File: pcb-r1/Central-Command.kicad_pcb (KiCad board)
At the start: 4 copper layers, 38.1 x 63.5 mm, 58 parts, among them P101 CONN_01X10, P102 CONN_01X10, P103 CONN_01X04, P104 CONN_01X02, P105 CONN_01X04, P106 CONN_01X02, P201 CONN_01X06, P202 CONN_01X04, P203 CONN_01X04, P204 CONN_01X03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

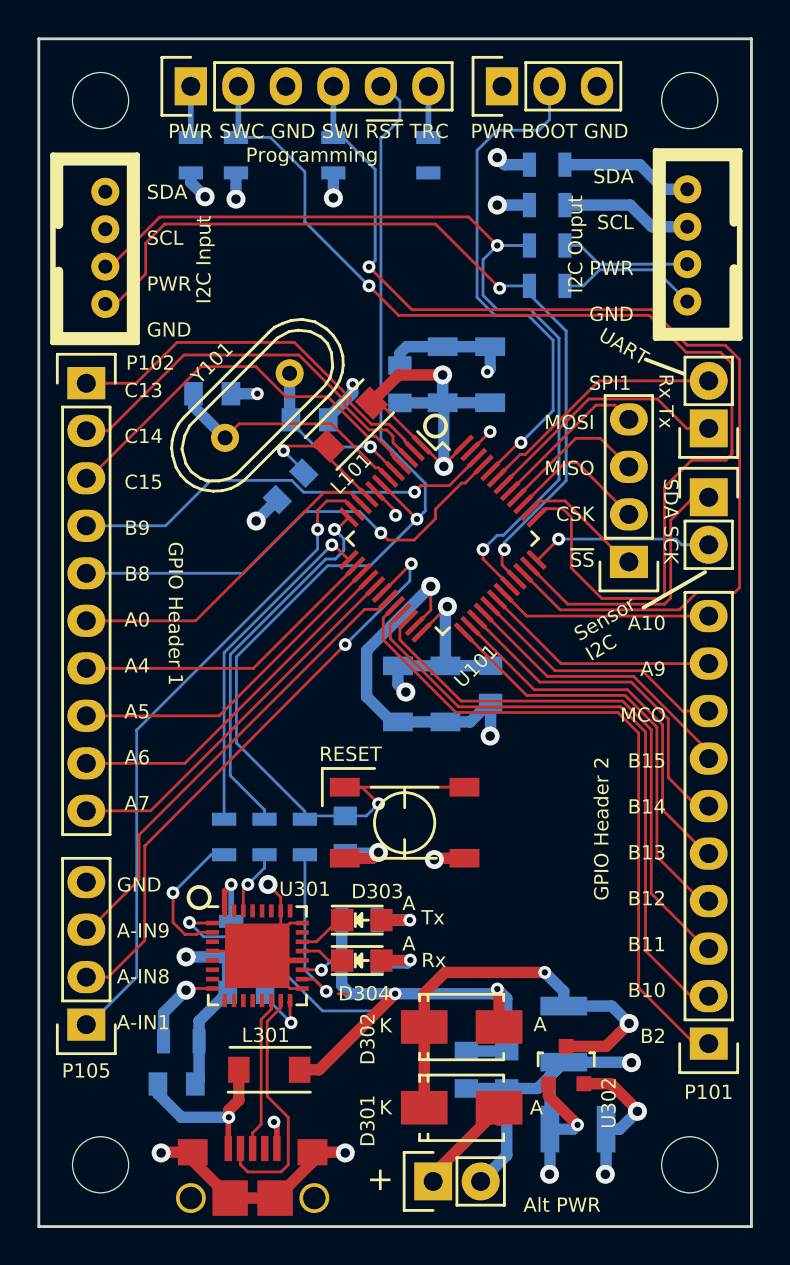
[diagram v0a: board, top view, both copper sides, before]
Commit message: Generated the final Gerbers for fabrication
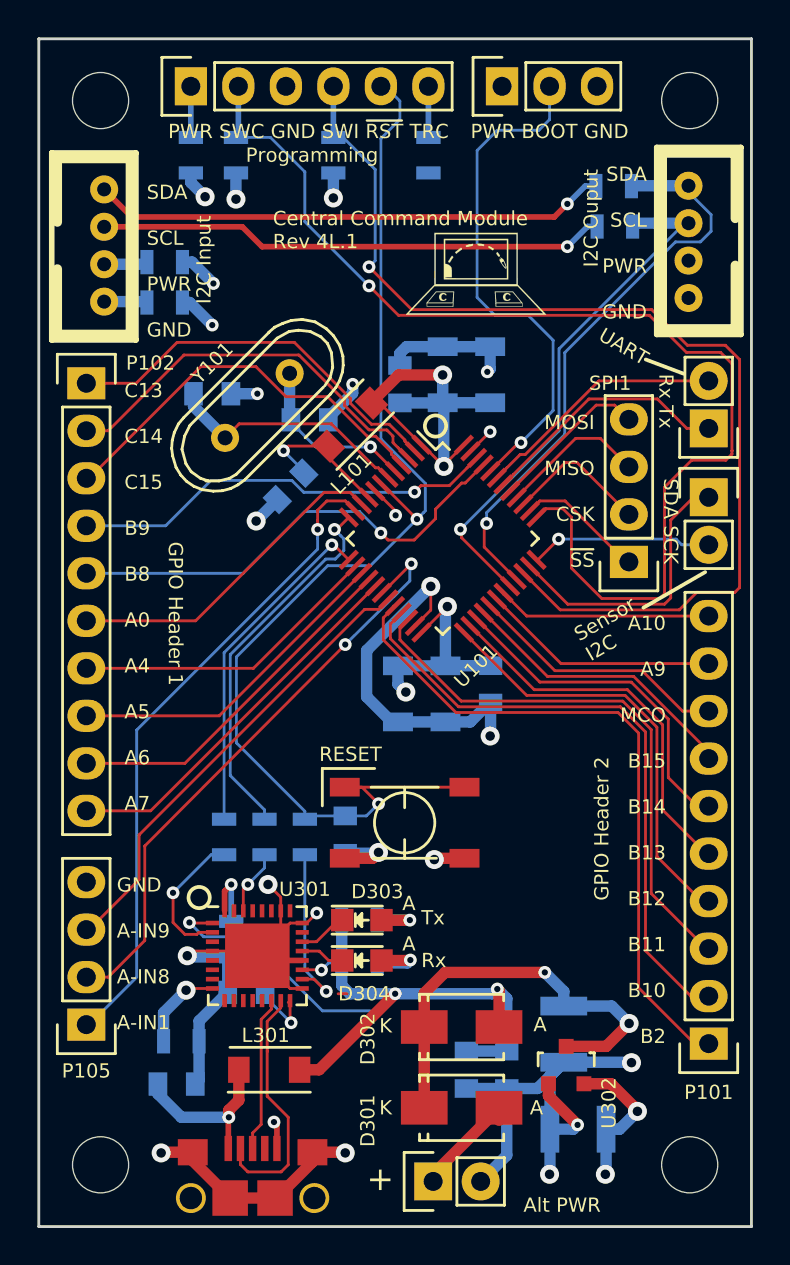
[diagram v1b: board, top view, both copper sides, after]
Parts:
- added G***: LOGO, CentralCommand:logo2, B.Cu at (102.5, 121.0)
- added G***: LOGO, CentralCommand:logo3, F.Cu at (99.6, 88.7)
- moved P203 31.8 mm to (79.7, 84.2), turned to 270 degrees
- moved P202 31.7 mm to (110.9, 90.1), turned to 90 degrees
- moved R206 21.7 mm to (82.9, 90.3), turned to 0 degrees
- moved R207 20.7 mm to (82.9, 88.1), turned to 0 degrees
- moved R209 6.41 mm to (106.9, 84.1), turned to 0 degrees
- moved R208 3.76 mm to (107.0, 86.2), turned to 0 degrees
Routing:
- net Net-(P203-Pad2): track 6.96 -> 27.5 mm, vias 0 -> 1
- net Net-(P203-Pad1): track 7.60 -> 27.6 mm, vias 0 -> 1
- net /Comm/SCL: track 48.2 -> 29.7 mm, vias 2 -> 1
- net /Comm/SDA: track 45.8 -> 31.1 mm, vias 2 -> 1
- net Net-(P203-Pad3): track 7.76 -> 2.62 mm
- net Net-(P203-Pad4): track 7.09 -> 3.50 mm
- net GND: track 109.4 -> 112.9 mm, vias 20 -> 21

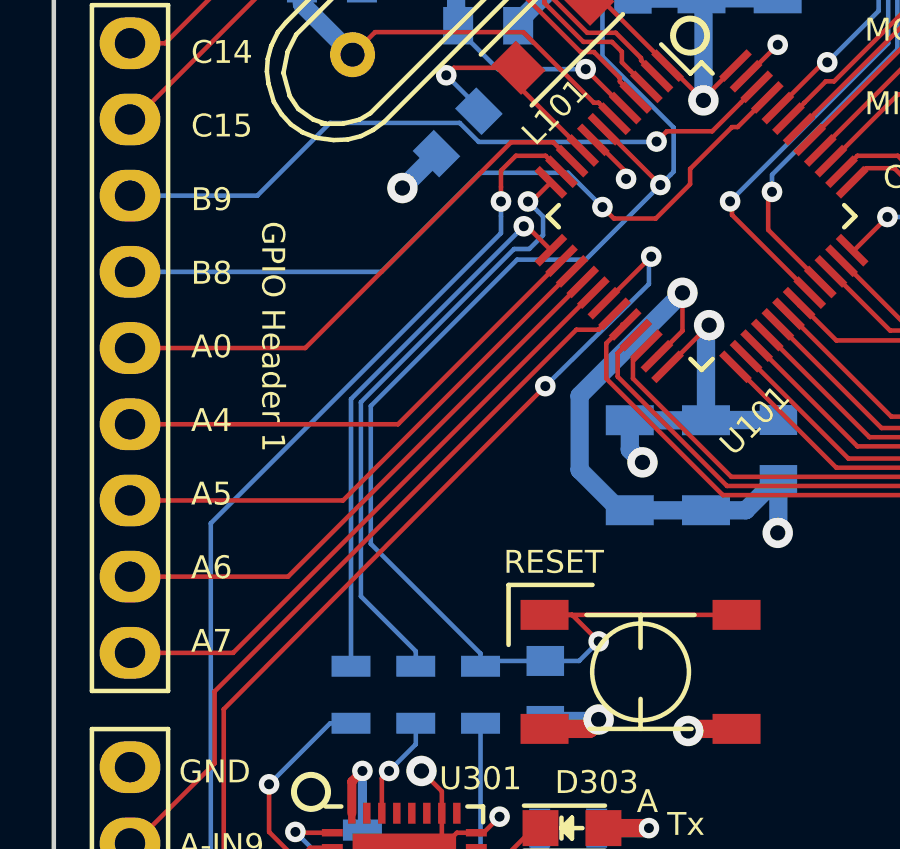
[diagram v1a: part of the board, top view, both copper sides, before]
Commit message: Corrected the routing of the Tx and Rx
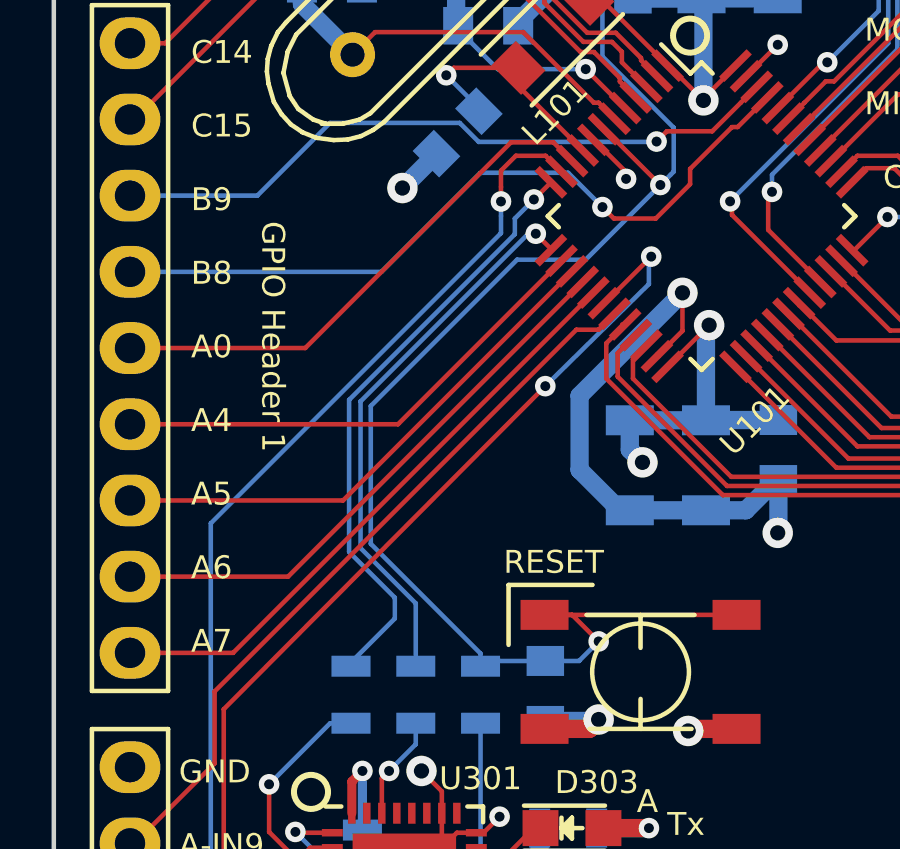
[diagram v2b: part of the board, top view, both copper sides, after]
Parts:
- C101, C201: value C -> 0.1μF
- C301: value 0.01μF -> 0.1μF
- R201, R202: value R -> 10kΩ
- R204: value 0Ω -> 10kΩ
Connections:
- U101 pad 12: /Power/TXD -> /Power/RXD
- U101 pad 13: /Power/RXD -> /Power/TXD
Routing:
- net /Power/RXD: track 18.3 -> 20.2 mm
- net /Power/TXD: track 20.6 -> 18.9 mm
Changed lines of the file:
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@@
     (thickness 1.6)
     (drawings 37)
-    (tracks 685)
+    (tracks 687)
     (zones 0)
     (modules 60)
@@
       (net 34 /ADC_IN1))
     (pad 12 smd rect (at -4.35 2.75 315) (size 1.3 0.25) (layers F.Cu F.Paste F.Mask)
-      (net 49 /Power/TXD))
-    (pad 13 smd rect (at -2.75 4.35 45) (size 1.3 0.25) (layers F.Cu F.Paste F.Mask)
       (net 51 /Power/RXD))
+    (pad 13 smd rect (at -2.75 4.35 45) (size 1.3 0.25) (layers F.Cu F.Paste F.Mask)
+      (net 49 /Power/TXD))
     (pad 14 smd rect (at -2.25 4.35 45) (size 1.3 0.25) (layers F.Cu F.Paste F.Mask)
       (net 27 "Net-(P102-Pad7)"))
@@
       (effects (font (size 0.762 0.762) (thickness 0.127)) (justify mirror))
     )
-    (fp_text value C (at 0 -2.1 225) (layer B.Fab)
+    (fp_text value 0.1μF (at 0 -2.1 225) (layer B.Fab)
       (effects (font (size 0.762 0.762) (thickness 0.127)) (justify mirror))
     )
@@
       (effects (font (size 0.762 0.762) (thickness 0.127)) (justify mirror))
     )
-    (fp_text value C (at 0 -2.1 270) (layer B.Fab)
+    (fp_text value 0.1μF (at 0 -2.1 270) (layer B.Fab)
       (effects (font (size 0.762 0.762) (thickness 0.127)) (justify mirror))
     )
@@
       (effects (font (size 0.762 0.762) (thickness 0.127)) (justify mirror))
     )
-    (fp_text value 0.01μF (at 0 -2.1) (layer B.Fab)
+    (fp_text value 0.1μF (at 0 -2.1) (layer B.Fab)
       (effects (font (size 0.762 0.762) (thickness 0.127)) (justify mirror))
     )
@@
       (effects (font (size 0.762 0.762) (thickness 0.127)) (justify mirror))
     )
-    (fp_text value R (at 0 -2.1 270) (layer B.Fab)
+    (fp_text value 10kΩ (at 0 -2.1 270) (layer B.Fab)
       (effects (font (size 0.762 0.762) (thickness 0.127)) (justify mirror))
     )
@@
       (effects (font (size 0.762 0.762) (thickness 0.127)) (justify mirror))
     )
-    (fp_text value R (at 0 -2.1 90) (layer B.Fab)
+    (fp_text value 10kΩ (at 0 -2.1 90) (layer B.Fab)
       (effects (font (size 0.762 0.762) (thickness 0.127)) (justify mirror))
     )
@@
       (effects (font (size 0.762 0.762) (thickness 0.127)) (justify mirror))
     )
-    (fp_text value 0Ω (at 0 -2.1 90) (layer B.Fab)
+    (fp_text value 10kΩ (at 0 -2.1 90) (layer B.Fab)
       (effects (font (size 0.762 0.762) (thickness 0.127)) (justify mirror))
     )
@@
   (segment (start 91.567 127.127) (end 90.912 126.472) (width 0.1524) (layer F.Cu) (net 48))
   (segment (start 90.912 126.472) (end 90.284 126.472) (width 0.1524) (layer F.Cu) (net 48))
-  (segment (start 92.769542 101.789429) (end 92.129439 102.429532) (width 0.1524) (layer F.Cu) (net 49))
-  (segment (start 88.265 117.4196) (end 86.4362 115.5908) (width 0.1524) (layer B.Cu) (net 49))
-  (segment (start 92.0496 104.013) (end 92.5068 103.5558) (width 0.1524) (layer B.Cu) (net 49))
-  (segment (start 92.348747 102.772431) (end 92.005848 102.429532) (width 0.1524) (layer B.Cu) (net 49))
-  (segment (start 86.4362 109.1184) (end 91.5416 104.013) (width 0.1524) (layer B.Cu) (net 49))
-  (via (at 92.005848 102.429532) (size 0.6858) (drill 0.3302) (layers F.Cu B.Cu) (net 49))
-  (segment (start 88.265 117.922) (end 88.265 117.4196) (width 0.1524) (layer B.Cu) (net 49))
-  (segment (start 92.5068 102.930484) (end 92.348747 102.772431) (width 0.1524) (layer B.Cu) (net 49))
-  (segment (start 86.4362 115.5908) (end 86.4362 109.1184) (width 0.1524) (layer B.Cu) (net 49))
-  (segment (start 92.5068 103.5558) (end 92.5068 102.930484) (width 0.1524) (layer B.Cu) (net 49))
-  (segment (start 92.129439 102.429532) (end 92.005848 102.429532) (width 0.1524) (layer F.Cu) (net 49))
-  (segment (start 91.5416 104.013) (end 92.0496 104.013) (width 0.1524) (layer B.Cu) (net 49))
+  (segment (start 88.265 117.922) (end 88.265 115.824) (width 0.1524) (layer B.Cu) (net 49) (status 400000))
+  (segment (start 92.2655 103.505) (end 92.769542 104.009042) (width 0.1524) (layer F.Cu) (net 49) (status 800000))
+  (via (at 92.2655 103.505) (size 0.6858) (drill 0.3302) (layers F.Cu B.Cu) (net 49))
+  (segment (start 92.0115 103.505) (end 92.2655 103.505) (width 0.1524) (layer B.Cu) (net 49))
+  (segment (start 86.4235 109.093) (end 92.0115 103.505) (width 0.1524) (layer B.Cu) (net 49))
+  (segment (start 86.4235 113.9825) (end 86.4235 109.093) (width 0.1524) (layer B.Cu) (net 49))
+  (segment (start 88.265 115.824) (end 86.4235 113.9825) (width 0.1524) (layer B.Cu) (net 49))
+  (segment (start 92.769542 104.009042) (end 92.769542 104.052171) (width 0.1524) (layer F.Cu) (net 49) (status C00000))
   (segment (start 88.265 117.922) (end 87.95 117.922) (width 0.1524) (layer B.Cu) (net 49))
+  (segment (start 92.769542 104.004258) (end 92.769542 104.052171) (width 0.1524) (layer F.Cu) (net 49))
   (segment (start 88.265 119.822) (end 88.265 120.523) (width 0.1524) (layer B.Cu) (net 50))
   (segment (start 87.134 121.654) (end 87.134 122.822) (width 0.1524) (layer F.Cu) (net 50))
@@
   (via (at 87.376 121.412) (size 0.6858) (drill 0.3302) (layers F.Cu B.Cu) (net 50))
   (segment (start 88.265 120.523) (end 87.376 121.412) (width 0.1524) (layer B.Cu) (net 50))
-  (segment (start 91.973478 103.256107) (end 91.866663 103.256107) (width 0.1524) (layer F.Cu) (net 51))
-  (segment (start 92.769542 104.052171) (end 91.973478 103.256107) (width 0.1524) (layer F.Cu) (net 51))
-  (segment (start 86.106 109.01677) (end 91.866663 103.256107) (width 0.1524) (layer B.Cu) (net 51))
-  (segment (start 86.106 117.922) (end 86.106 109.01677) (width 0.1524) (layer B.Cu) (net 51))
-  (via (at 91.866663 103.256107) (size 0.6858) (drill 0.3302) (layers F.Cu B.Cu) (net 51))
-  (segment (start 92.769542 104.004258) (end 92.769542 104.052171) (width 0.1524) (layer F.Cu) (net 51))
+  (segment (start 86.106 117.922) (end 86.106 117.7925) (width 0.1524) (layer B.Cu) (net 51) (status C00000))
+  (segment (start 86.106 117.7925) (end 87.5665 116.332) (width 0.1524) (layer B.Cu) (net 51) (status 400000))
+  (segment (start 87.5665 116.332) (end 87.5665 115.6335) (width 0.1524) (layer B.Cu) (net 51))
+  (segment (start 87.5665 115.6335) (end 86.0425 114.1095) (width 0.1524) (layer B.Cu) (net 51))
+  (segment (start 86.0425 114.1095) (end 86.0425 109.042944) (width 0.1524) (layer B.Cu) (net 51))
+  (segment (start 86.0425 109.042944) (end 91.567 103.518444) (width 0.1524) (layer B.Cu) (net 51))
+  (segment (start 91.567 103.518444) (end 91.567 102.997) (width 0.1524) (layer B.Cu) (net 51))
+  (segment (start 91.567 102.997) (end 92.202 102.362) (width 0.1524) (layer B.Cu) (net 51))
+  (via (at 92.202 102.362) (size 0.6858) (drill 0.3302) (layers F.Cu B.Cu) (net 51))
+  (segment (start 92.202 102.362) (end 92.769542 101.794458) (width 0.1524) (layer F.Cu) (net 51) (status 800000))
+  (segment (start 92.769542 101.794458) (end 92.769542 101.789429) (width 0.1524) (layer F.Cu) (net 51) (status C00000))
   (segment (start 85.484 123.972) (end 84.7525 123.972) (width 0.1524) (layer F.Cu) (net 52))
   (segment (start 85.41 119.822) (end 86.106 119.822) (width 0.1524) (layer B.Cu) (net 52))
